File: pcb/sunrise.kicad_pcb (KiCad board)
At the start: 2 copper layers, 52.1 x 29.2 mm, 20 parts, among them J1 Conn_01x15_Female, J2 Conn_01x15_Female, J3 Conn_01x04_Female, J4 Conn_01x02_Female, Q1 TSM2302CX, Q2 TSM2302CX, Q3 TSM2302CX, SW1 SW_SPDT, U1 MCP1703A-5002_SOT223, U2 TSOP312xx

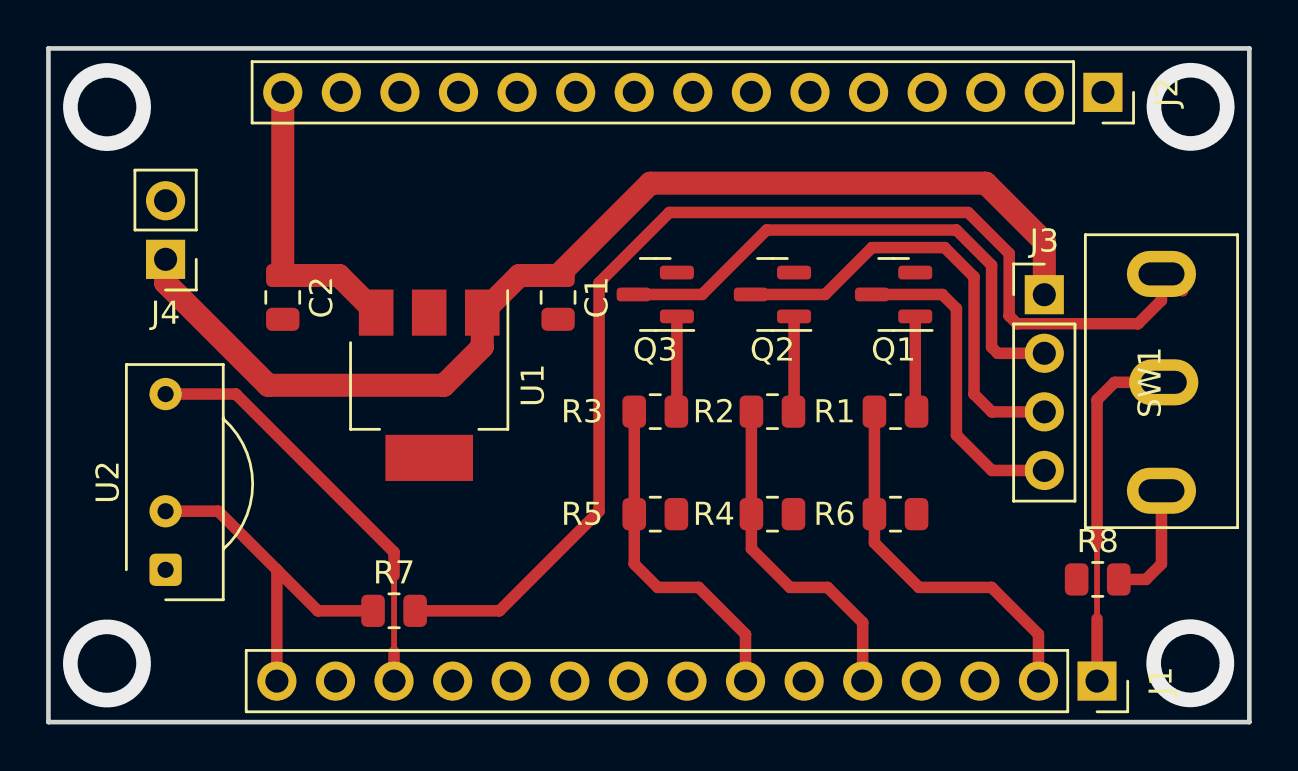
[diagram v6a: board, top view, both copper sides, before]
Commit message: Corrected component positions
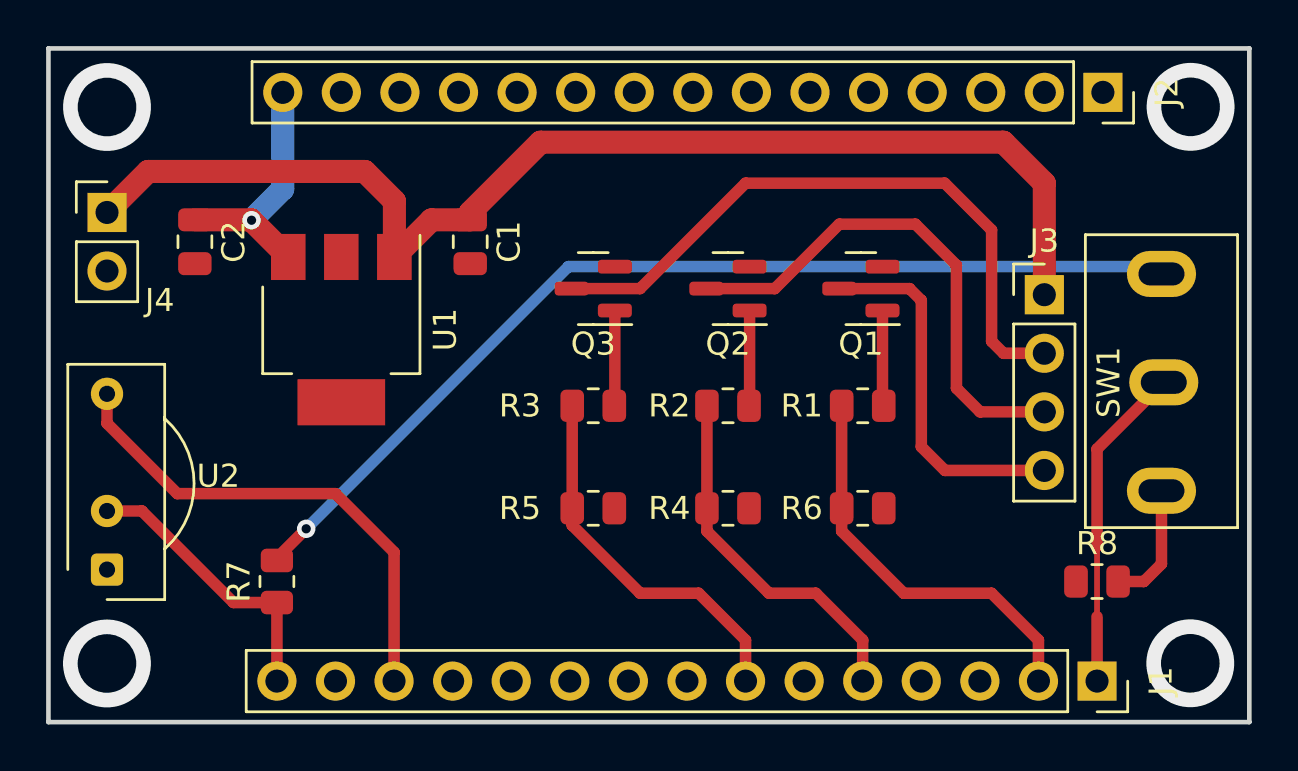
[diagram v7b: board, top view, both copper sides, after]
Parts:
- moved R7 5.24 mm to (84.8, 95.5), turned to 90 degrees
- moved U1 4.51 mm to (87.6, 84.6)
- moved C1 4.51 mm to (93.2, 80.8)
- moved C2 4.51 mm to (81.3, 80.8)
- moved J4 3.25 mm to (77.5, 79.5), turned to 0 degrees
- moved Q3 2.70 mm to (98.6, 82.8)
- moved R3 2.70 mm to (98.6, 87.9)
- moved R5 2.70 mm to (98.6, 92.3)
- moved U2 2.54 mm to (77.5, 95.0)
- moved Q2 1.95 mm to (104.4, 82.8)
- moved R2 1.95 mm to (104.4, 87.9)
- moved R4 1.95 mm to (104.4, 92.3)
- moved Q1 1.44 mm to (110.2, 82.8)
- moved R1 1.44 mm to (110.2, 87.9)
- moved R6 1.44 mm to (110.2, 92.3)
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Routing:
- net Net-(R7-Pad2): track 51.2 -> 43.8 mm, vias 0 -> 1
- net Net-(J3-Pad2): track 23.3 -> 28.3 mm
- net +12V: track 48.8 -> 52.2 mm
- net /IR_D: track 18.3 -> 21.6 mm
- net /+3.3V: track 15.6 -> 12.4 mm
- net Net-(J3-Pad3): track 19.5 -> 22.3 mm
- net Net-(J3-Pad4): track 13.8 -> 15.9 mm
- net +5V: track 12.7 -> 10.8 mm, vias 0 -> 1
- net /BLUE_IO: track 14.7 -> 16.5 mm
- net /GREEN_IO: track 14.6 -> 15.9 mm
- net /ALARM_EN: track 15.4 -> 14.2 mm
- net /RED_IO: track 16.5 -> 17.7 mm

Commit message: Changed traces
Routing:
- net Net-(R7-Pad2): track 43.8 -> 51.1 mm
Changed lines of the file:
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@@
   (segment (start 84.836 94.5915) (end 84.836 94.488) (width 0.5) (layer "F.Cu") (net 37))
   (via (at 86.106 93.218) (size 0.8) (drill 0.4) (layers "F.Cu" "B.Cu") (net 37))
+  (segment (start 94.996 84.328) (end 94.996 80.01) (width 0.5) (layer "B.Cu") (net 37))
+  (segment (start 117.73 76.708) (end 123.19 82.168) (width 0.5) (layer "B.Cu") (net 37))
   (segment (start 122.87 81.848) (end 123.19 82.168) (width 0.5) (layer "B.Cu") (net 37))
-  (segment (start 86.106 93.218) (end 97.476 81.848) (width 0.5) (layer "B.Cu") (net 37))
-  (segment (start 97.476 81.848) (end 122.87 81.848) (width 0.5) (layer "B.Cu") (net 37))
+  (segment (start 98.298 76.708) (end 117.73 76.708) (width 0.5) (layer "B.Cu") (net 37))
+  (segment (start 86.106 93.218) (end 94.996 84.328) (width 0.5) (layer "B.Cu") (net 37))
+  (segment (start 94.996 80.01) (end 98.298 76.708) (width 0.5) (layer "B.Cu") (net 37))
   (segment (start 122.428 95.504) (end 123.19 94.742) (width 0.5) (layer "F.Cu") (net 38))
   (segment (start 121.3085 95.504) (end 122.428 95.504) (width 0.5) (layer "F.Cu") (net 38))
